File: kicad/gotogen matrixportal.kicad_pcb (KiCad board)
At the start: 2 copper layers, 139.7 x 63.5 mm, 27 parts, among them J1 HUB75 Out, J2 HUB75 In, J3 OLED_128_64, J4 Buttons EXT, J5 OpenMV, J6 Extra Connections, J7 Capacitive Touch, SW1 Back, SW2 Menu, SW3 Up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

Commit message: first pass at pcb update
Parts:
- added SW7: Reset, Button_Switch_THT:SW_PUSH_6mm, F.Cu at (78.0, 66.3)
- J6: footprint Connector_PinHeader_2.54mm:PinHeader_1x06_P2.54mm_Vertical -> Connector_PinHeader_2.54mm:PinHeader_1x05_P2.54mm_Vertical
- moved JP3 131.4 mm to (181.6, 104.2), turned to 90 degrees
- moved JP2 123.8 mm to (177.8, 109.2), turned to 180 degrees
- moved J6 101.6 mm to (147.3, 99.1), turned to -90 degrees
- moved C1 97.7 mm to (129.5, 54.6)
- moved C2 97.7 mm to (134.6, 54.6)
- moved R1 97.7 mm to (124.5, 61.0)
- moved R2 96.8 mm to (119.4, 61.0)
- moved R3 96.0 mm to (114.3, 61.0)
- moved U3 95.6 mm to (139.7, 61.0)
- moved U5 94.9 mm to (173.9, 100.9), turned to -90 degrees
- moved JP4 94.5 mm to (129.5, 100.3)
- moved U1 83.1 mm to (87.1, 63.6)
- moved SW3 81.0 mm to (143.4, 124.8)
- moved SW4 80.7 mm to (143.4, 134.9)
- moved J2 78.4 mm to (118.1, 137.2)
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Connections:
- net /A_GAIN renamed /GAIN
- J6 pad 2: /PA07 -> /PB13
- J6 pad 3: /PB13 -> /PB14
- J6 pad 4: /PB14 -> /PB07
- J6 pad 5: /PB07 -> GND
- JP2 pad 1: /A_GND -> GND
- JP2 pad 3: /A_VDD -> +3.3V
- JP3 pad 1: /A_GND -> GND
- JP3 pad 3: /A_VDD -> +3.3V
- U1 pad 1: unconnected-(U1-Pad1) -> Net-(SW7-Pad2)
- U1 pad 9: /PA07 -> /MIC
- U2 pad 2: unconnected-(U2-Pad2) -> GND
- U5 pad 1: /A_GND -> GND
- U5 pad 2: /A_VDD -> +3.3V
- U5 pad 4: unconnected-(U5-Pad4) -> /MIC
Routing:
- net /MIC: track 0.00 -> 87.6 mm, vias 0 -> 2
- net /LOOP_R2: track 63.9 -> 124.3 mm
- net /PA07: track 59.4 -> 0.00 mm
- net /B_BACK: track 109.1 -> 59.8 mm
- net /CAM_RX: track 172.7 -> 217.2 mm
- net /LOOP_G2: track 61.7 -> 104.4 mm
- net /CAM_TX: track 175.0 -> 215.9 mm
- net /OLED_DATA: track 129.7 -> 88.8 mm
- net /OLED_CLK: track 130.5 -> 90.7 mm
- net /LOOP_R1: track 60.2 -> 98.6 mm
- net /LOOP_G1: track 51.5 -> 87.1 mm
- net /B_EXTRA2: track 44.9 -> 74.9 mm
- net /LOOP_B1: track 58.8 -> 88.7 mm
- net /A_GND: track 29.6 -> 0.00 mm
- net /M_A: track 38.6 -> 67.7 mm
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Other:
- board size 139.7 x 63.5 mm -> 139.7 x 110.1 mm
- board text added: "3V3 PB13 (Out, 5V) PB14 (Out, 5V) PB07 (Out, 5V) GND"
- board text added: "GND Extra 3 Extra 2 Extra 1 Down Up Menu Back"
- board text added: "Gotogen MatrixPortal v0.2 © 2023 Andy Janata CC-BY-SA https://elbrarc.at/"
- board text removed: "3V3 PA07 (I/O, 3V3) PB13 (Out, 5V) PB14 (Out, 5V) PB07 (Out, 5V) GND"
- board text removed: "GND -- Extra 3 Extra 2 Extra 1 Down Up Menu Back"
- board text removed: "Gotogen MatrixPortal v0.1 © 2022 Andy Janata CC-BY-SA https://elbrarc.at/"

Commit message: further pcb updates
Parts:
- moved R3 30.8 mm to (142.9, 49.5)
- moved SW7 29.5 mm to (85.2, 95.0), turned to 180 degrees
- moved R2 29.0 mm to (146.1, 49.5)
- moved R1 27.3 mm to (149.2, 49.5)
- moved SW6 22.9 mm to (182.2, 54.3)
- moved SW5 22.3 mm to (169.5, 54.3)
- moved U2 12.7 mm to (132.0, 63.4)
- moved C1 11.4 mm to (139.7, 49.5), turned to 90 degrees
- moved C2 5.50 mm to (136.5, 49.5), turned to 90 degrees
- moved J3 0.06 mm to (155.5, 63.6)
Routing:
- net /CAM_RX: track 217.2 -> 141.7 mm, vias 0 -> 1
- net /CAM_TX: track 215.9 -> 142.8 mm, vias 0 -> 1
- net /I2C_SDA: track 152.9 -> 119.9 mm
- net /I2C_SCL: track 148.2 -> 121.7 mm
- net GND: track 45.5 -> 19.3 mm, vias 3 -> 1
- net /OLED_RST: track 137.9 -> 113.1 mm
- net /OLED_DC: track 145.6 -> 121.2 mm
- net /OLED_CS: track 131.9 -> 107.6 mm
- net /B_EXTRA1: track 78.7 -> 56.7 mm
- net /B_DOWN: track 113.1 -> 100.9 mm
- net /B_EXTRA2: track 74.9 -> 70.4 mm
- net +3.3V: track 252.4 -> 256.0 mm
- net /GPIO_INT: track 78.3 -> 81.4 mm
- net /LOOP_G2: track 104.4 -> 102.4 mm
- net /LOOP_R2: track 124.3 -> 122.3 mm
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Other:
- board size 139.7 x 110.1 mm -> 134 x 105.4 mm

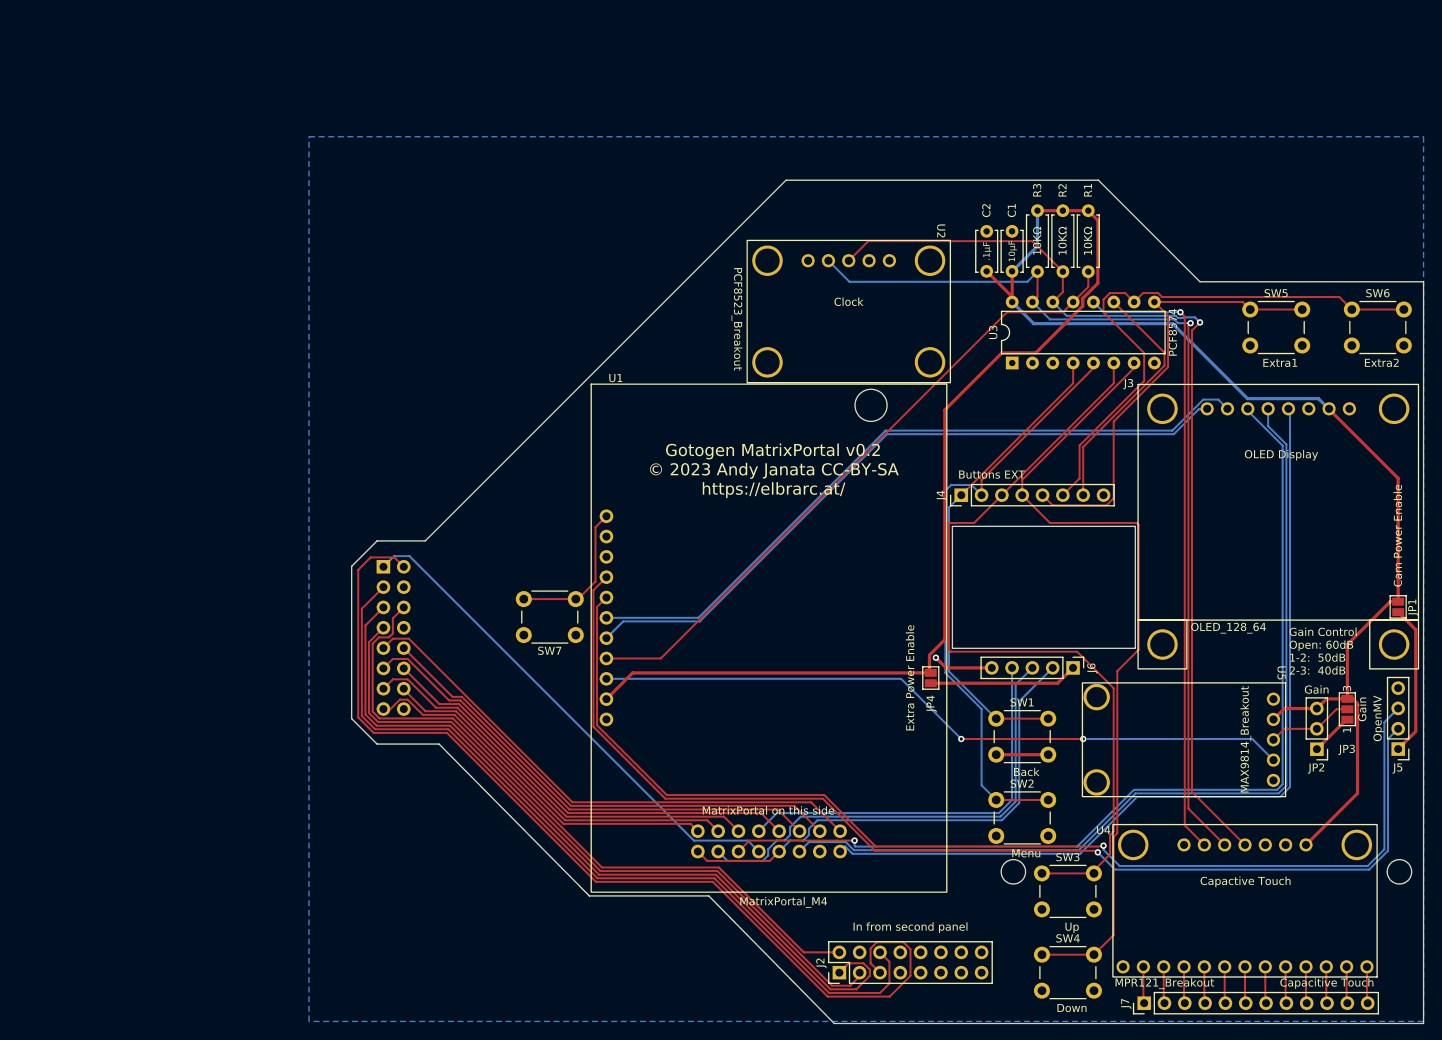
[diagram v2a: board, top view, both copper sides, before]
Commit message: completely rework PCB layout
needed to get the matrixportal further away from my face, which required
moving just about everything around
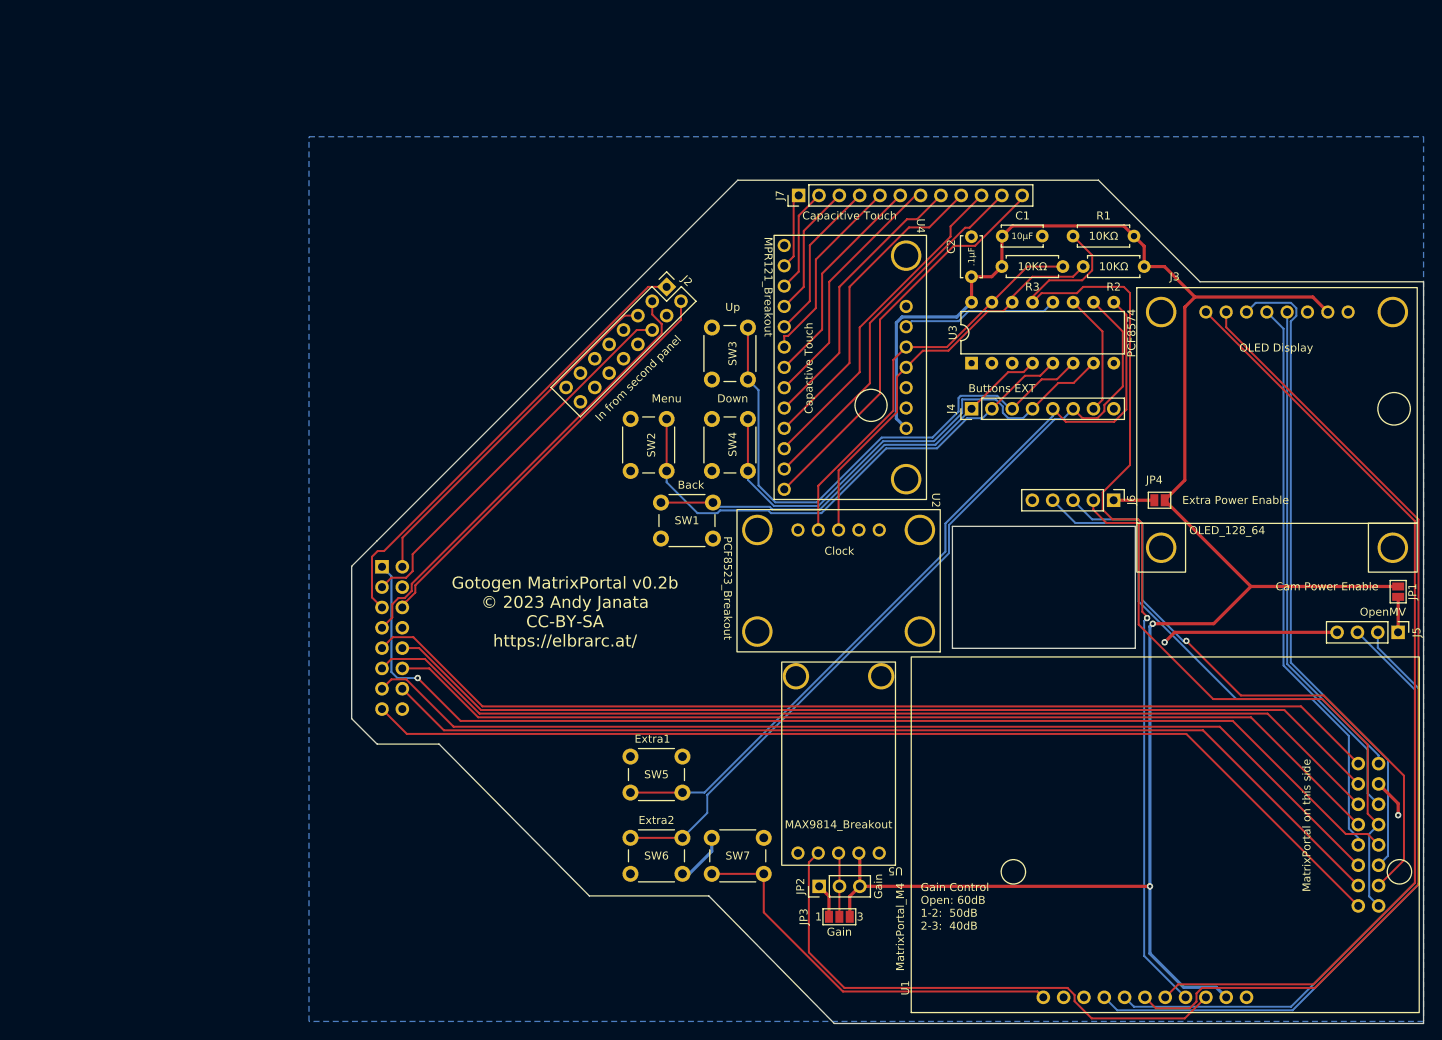
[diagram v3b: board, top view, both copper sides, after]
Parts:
- moved SW6 111.8 mm to (92.0, 120.3)
- moved J7 109.8 mm to (113.0, 40.0)
- moved U4 96.1 mm to (110.0, 78.0), turned to 90 degrees
- moved SW5 93.2 mm to (98.5, 114.6), turned to 180 degrees
- moved J2 88.4 mm to (96.5, 51.4), turned to -45 degrees
- moved U1 88.2 mm to (127.1, 142.1), turned to 90 degrees
- moved SW3 77.5 mm to (106.7, 56.5), turned to -90 degrees
- moved SW4 76.4 mm to (106.7, 67.9), turned to -90 degrees
- moved JP3 68.6 mm to (118.1, 130.2), turned to 0 degrees
- moved JP2 64.5 mm to (115.6, 126.4), turned to 90 degrees
- moved SW2 63.0 mm to (96.5, 67.9), turned to -90 degrees
- moved U5 53.8 mm to (125.1, 123.7), turned to 180 degrees
- moved SW1 49.9 mm to (95.8, 78.4)
- moved JP4 36.2 mm to (158.1, 78.1), turned to 180 degrees
- moved U2 33.7 mm to (130.7, 97.1)
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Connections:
- net Net-(SW7-Pad2) renamed /RESET
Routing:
- net /M_OE: track 45.9 -> 132.2 mm
- net /M_DATA: track 62.8 -> 146.0 mm, vias 0 -> 1
- net /M_LAT: track 46.7 -> 129.7 mm
- net /M_CLK: track 52.7 -> 132.1 mm
- net /LOOP_R2: track 122.3 -> 44.6 mm
- net /M_D: track 55.4 -> 127.6 mm
- net /I2C_SCL: track 121.7 -> 51.6 mm, vias 1 -> 0
- net /I2C_SDA: track 119.9 -> 51.2 mm, vias 1 -> 0
- net /M_C: track 61.4 -> 130.0 mm
- net /M_B: track 61.5 -> 126.5 mm
- net /CAM_RX: track 141.7 -> 77.5 mm, vias 1 -> 0
- net /CAM_TX: track 142.8 -> 80.1 mm, vias 1 -> 0
- net /M_A: track 67.5 -> 129.1 mm
- net /CT_INT: track 79.2 -> 19.6 mm, vias 1 -> 0
- net /LOOP_G2: track 102.4 -> 48.3 mm
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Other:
- outline, holes or cut-outs redrawn
- board text added: "Gotogen MatrixPortal v0.2b © 2023 Andy Janata CC-BY-SA https://elbrarc.at/"
- board text removed: "Connect directly to input of first panel"
- board text removed: "Gotogen MatrixPortal v0.2 © 2023 Andy Janata CC-BY-SA https://elbrarc.at/"

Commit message: move mounting holes
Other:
- outline, holes or cut-outs redrawn
- board text added: "Gotogen MatrixPortal v0.3 © 2023 Andy Janata CC-BY-SA https://elbrarc.at/"
- board text removed: "Gotogen MatrixPortal v0.2b © 2023 Andy Janata CC-BY-SA https://elbrarc.at/"
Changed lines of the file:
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@@
     )
   )
-  (gr_circle (center 188.121524 124.552476) (end 189.645524 124.552476) (layer "F.SilkS") (width 0.1) (fill none))
-  (gr_circle (center 139.861524 124.552476) (end 141.385524 124.552476) (layer "F.SilkS") (width 0.1) (fill none))
-  (gr_circle (center 187.452 66.675) (end 189.484 66.675) (layer "F.SilkS") (width 0.1) (fill none))
-  (gr_circle (center 122.0724 66.2432) (end 124.079 66.2432) (layer "F.SilkS") (width 0.1) (fill none))
+  (gr_circle (center 188.121524 139.065) (end 189.645524 139.065) (layer "Edge.Cuts") (width 0.1) (fill none))
   (gr_line (start 57.15 86.36) (end 57.15 105.41) (layer "Edge.Cuts") (width 0.1))
   (gr_line (start 68.072 108.585) (end 60.325 108.585) (layer "Edge.Cuts") (width 0.1))
@@
   (gr_line (start 60.325 83.185) (end 105.41 38.1) (layer "Edge.Cuts") (width 0.1))
   (gr_line (start 163.195 50.8) (end 191.135 50.8) (layer "Edge.Cuts") (width 0.1))
+  (gr_circle (center 129.54 136.525) (end 131.064 136.525) (layer "Edge.Cuts") (width 0.1) (fill none))
   (gr_line (start 150.495 38.1) (end 105.41 38.1) (layer "Edge.Cuts") (width 0.1))
   (gr_line (start 86.868 127.5715) (end 68.072 108.585) (layer "Edge.Cuts") (width 0.1))
@@
     (effects (font (size 1 1) (thickness 0.15)))
   )
-  (gr_text "Gotogen MatrixPortal v0.2b\n© 2023 Andy Janata\nCC-BY-SA\nhttps://elbrarc.at/" (at 83.82 92.075) (layer "F.SilkS")
+  (gr_text "Gotogen MatrixPortal v0.3\n© 2023 Andy Janata\nCC-BY-SA\nhttps://elbrarc.at/" (at 83.82 92.075) (layer "F.SilkS")
     (effects (font (size 1.5 1.5) (thickness 0.2)))
   )

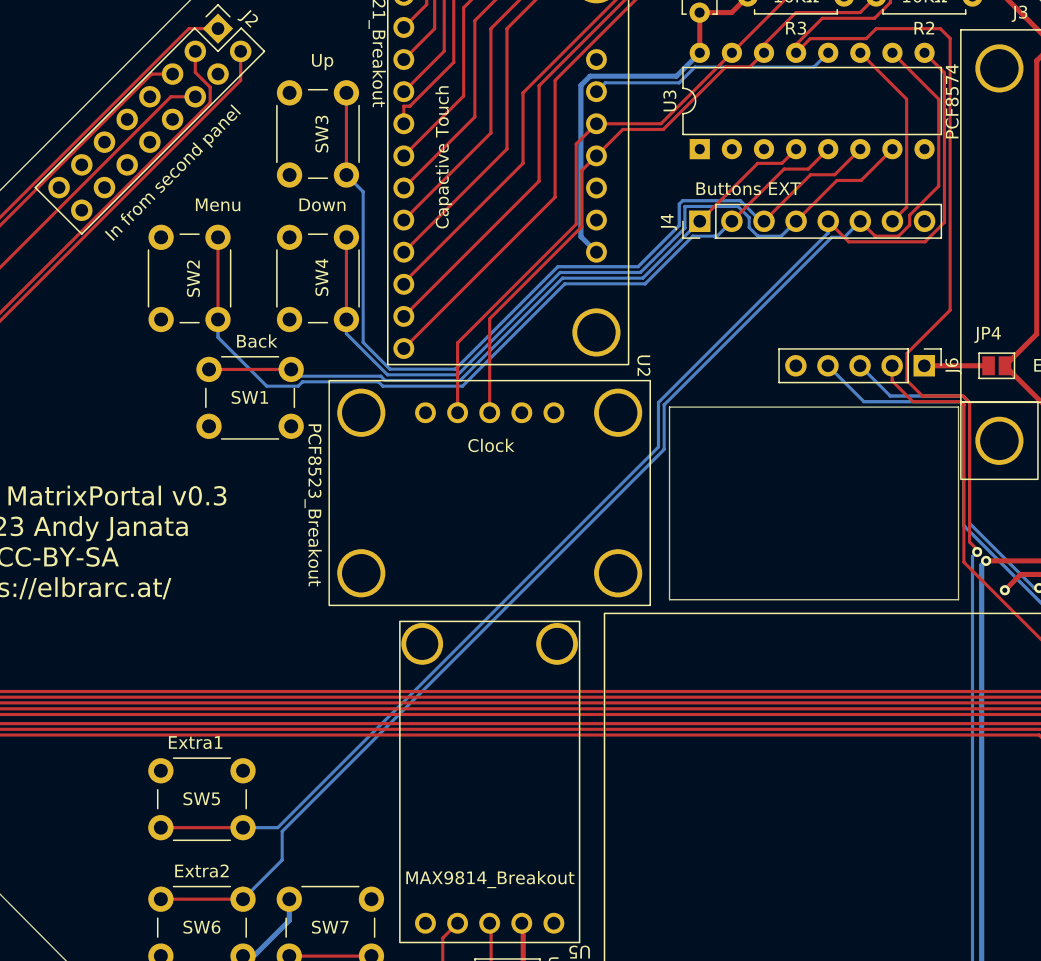
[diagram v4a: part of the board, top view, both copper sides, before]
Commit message: add some missing silkscreen
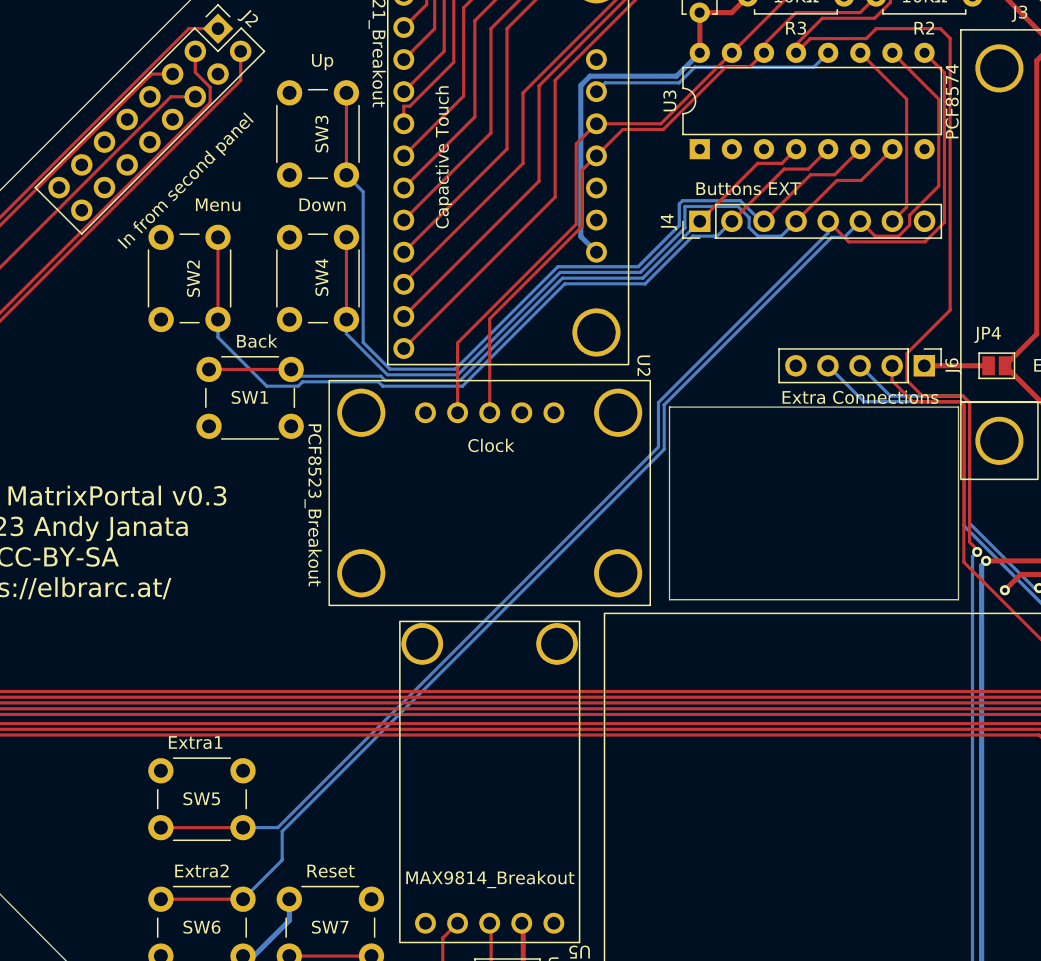
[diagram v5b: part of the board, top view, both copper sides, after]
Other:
- board text added: "Connect directly to first panel"
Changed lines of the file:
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@@
       (effects (font (size 1 1) (thickness 0.15)))
     )
-    (fp_text value "Extra Connections" (at 2.54 5.08) (layer "F.Fab")
+    (fp_text value "Extra Connections" (at 2.54 5.08) (layer "F.SilkS")
       (effects (font (size 1 1) (thickness 0.15)))
     )
@@
       (effects (font (size 1 1) (thickness 0.15)))
     )
-    (fp_text value "Reset" (at 3.25 -2.195) (layer "F.Fab")
+    (fp_text value "Reset" (at 3.25 -2.195) (layer "F.SilkS")
       (effects (font (size 1 1) (thickness 0.15)))
     )
@@
     (effects (font (size 1.6 1.6) (thickness 0.2)) (justify right mirror))
   )
-  (gr_text "In from second panel" (at 92.970324 62.865 45) (layer "F.SilkS")
+  (gr_text "Connect directly to first panel" (at 67.945 95.885 90) (layer "B.SilkS")
+    (effects (font (size 1 1) (thickness 0.15)) (justify mirror))
+  )
+  (gr_text "In from second panel" (at 93.98 63.5 45) (layer "F.SilkS")
     (effects (font (size 1 1) (thickness 0.15)))
   )
